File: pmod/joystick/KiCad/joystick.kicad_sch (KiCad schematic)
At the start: 9 parts, among them J2 Conn_01x05_Pin, U1 COM-09032

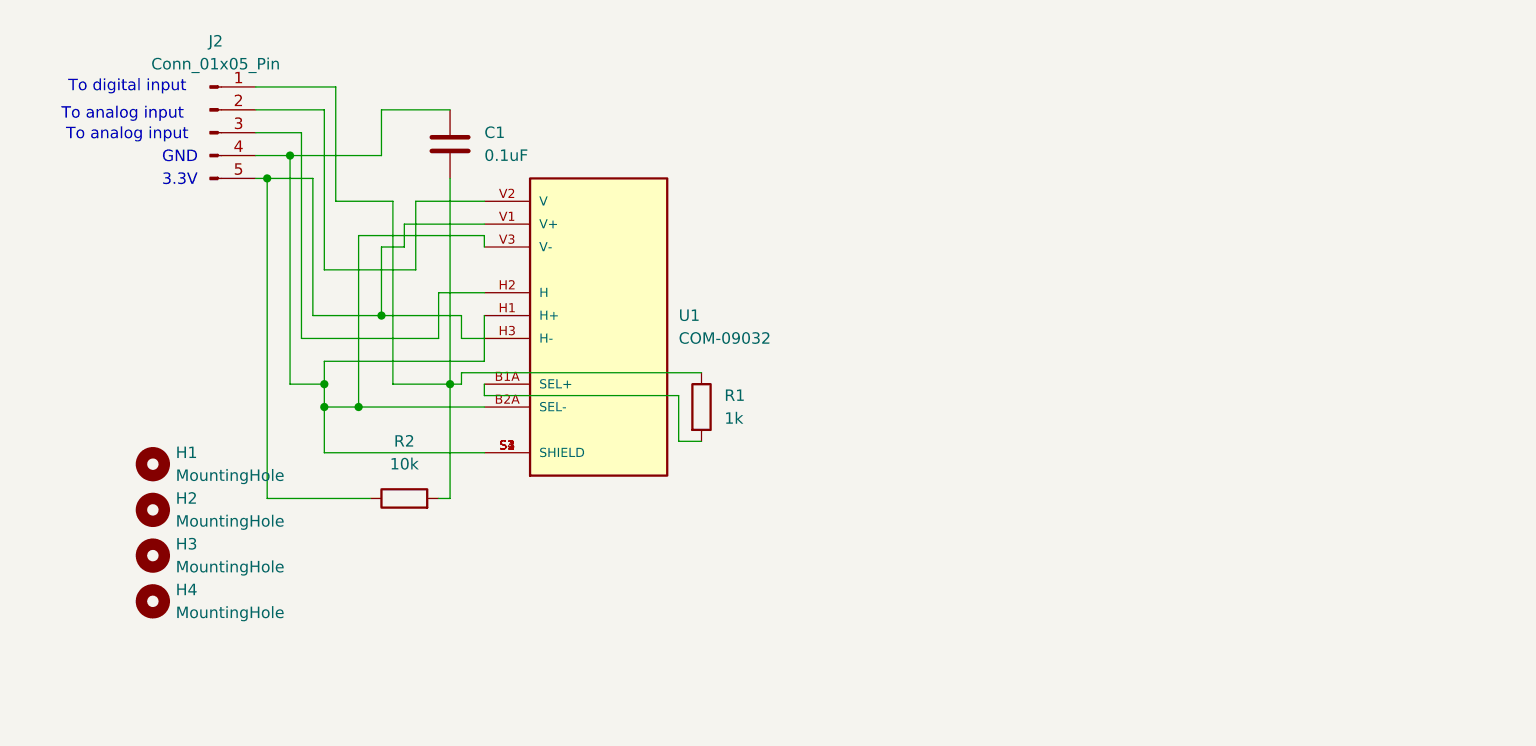
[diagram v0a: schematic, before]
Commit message: schematic and PCB added
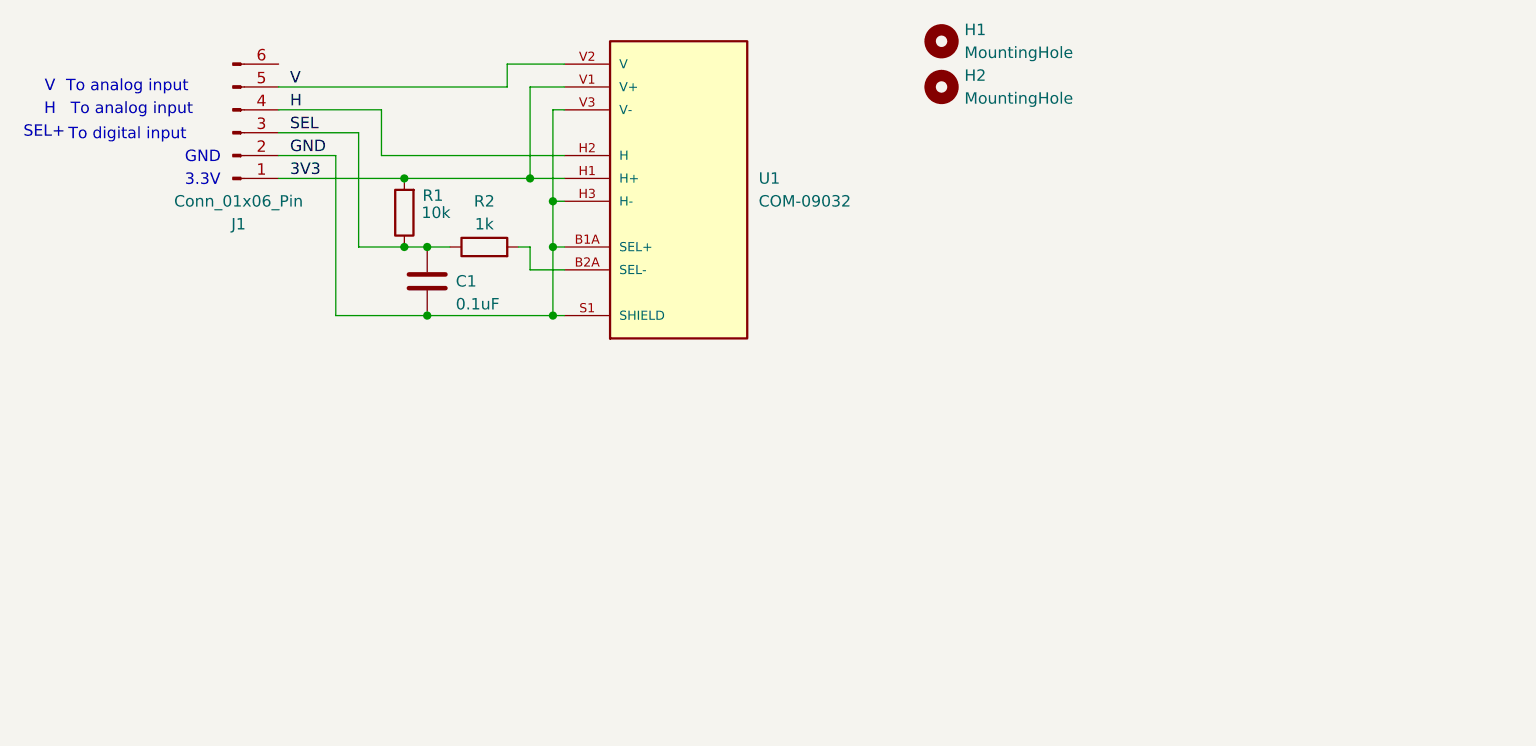
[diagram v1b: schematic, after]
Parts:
- removed H3, H4: MountingHole, MountingHole:MountingHole_3.2mm_M3_DIN965, symbol Mechanical:MountingHole
- removed J2: Conn_01x05_Pin, symbol Connector:Conn_01x05_Pin
- added J1: Conn_01x06_Pin, Connector_PinHeader_2.54mm:PinHeader_1x06_P2.54mm_Vertical, symbol Connector:Conn_01x06_Pin
- C1: footprint Capacitor_SMD:C_0603_1608Metric -> Capacitor_SMD:C_1206_3216Metric_Pad1.33x1.80mm_HandSolder
- H1, H2: now left out of the parts list
- R1: renamed from R2; footprint Resistor_SMD:R_0603_1608Metric_Pad0.98x0.95mm_HandSolder -> Resistor_SMD:R_1206_3216Metric_Pad1.30x1.75mm_HandSolder
- R2: renamed from R1; footprint Resistor_SMD:R_0603_1608Metric_Pad0.98x0.95mm_HandSolder -> Resistor_SMD:R_1206_3216Metric_Pad1.30x1.75mm_HandSolder
- U1: footprint XDCR_COM-09032 -> COM-09032:XDCR_COM-09032; Availability (none) -> In Stock; Check_prices (none) -> https://www.snapeda.com/parts/COM-09032/SparkFun/view-part/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; Description_1 (none) -> Joystick, 2 - Axis Analog (Resistive) Output; MF (none) -> SparkFun Electronics; MP (none) -> COM-09032; Package (none) -> Package; Price (none) -> None; SnapEDA_Link (none) -> https://www.snapeda.com/parts/COM-09032/SparkFun/view-part/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
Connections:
- net at R2.2: now also U1.B2A (SEL-); no longer U1.B1A (SEL+)
- net GND: now reaches U1.S1 (SHIELD), U1.S2 (SHIELD), U1.S3 (SHIELD), U1.S4 (SHIELD), U1.V3 (V-)
- net GND: now also C1.2, U1.B1A (SEL+), U1.H3 (H-), J1.2 (Pin_2); no longer C1.1, U1.B2A (SEL-), U1.H1 (H+)
- net H: now reaches U1.H2 (H)
- net H: now also J1.4 (Pin_4)
- net V: now reaches U1.V2 (V)
- net V: now also J1.5 (Pin_5)
- new net 3V3: J1.1 (Pin_1), R1.2, U1.H1 (H+), U1.V1 (V+)
- new net SEL: C1.1, J1.3 (Pin_3), R1.1, R2.1
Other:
- note added: "H"
- note added: "SEL+"
- note added: "V"
- moved on the sheet: C1, R1, R2

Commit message: fix: Pridal jsem opravy, ktere byly navrzene
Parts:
- added H3, H4: MountingHole, MountingHole:MountingHole_3.2mm_M3_DIN965, symbol Mechanical:MountingHole

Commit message: fix: prepare all board for manufacturing
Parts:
- H1, H2, H3, H4: footprint MountingHole:MountingHole_3.2mm_M3_DIN965 -> MountingHole:MountingHole_3.2mm_M3
- J1: footprint Connector_PinHeader_2.54mm:PinHeader_1x06_P2.54mm_Vertical -> Connector_PinHeader_2.54mm:PinHeader_1x06_P2.54mm_Horizontal
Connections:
- net SEL: now also J1.5 (Pin_5), U1.V2 (V); no longer C1.1, J1.3 (Pin_3), R1.1, R2.1
- net V: now also C1.1, J1.3 (Pin_3), R1.1, R2.1; no longer J1.5 (Pin_5), U1.V2 (V)
- no-connect marks 0 -> 1
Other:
- moved on the sheet: C1, H1, H2, H3, H4, J1, R1, R2, U1

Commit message: docs: add images, fix docs
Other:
- moved on the sheet: C1, H1, H2, H3, H4, J1, R1, R2, U1
